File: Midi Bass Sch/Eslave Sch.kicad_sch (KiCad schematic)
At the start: 11 parts, among them SW1 E-slave Reset

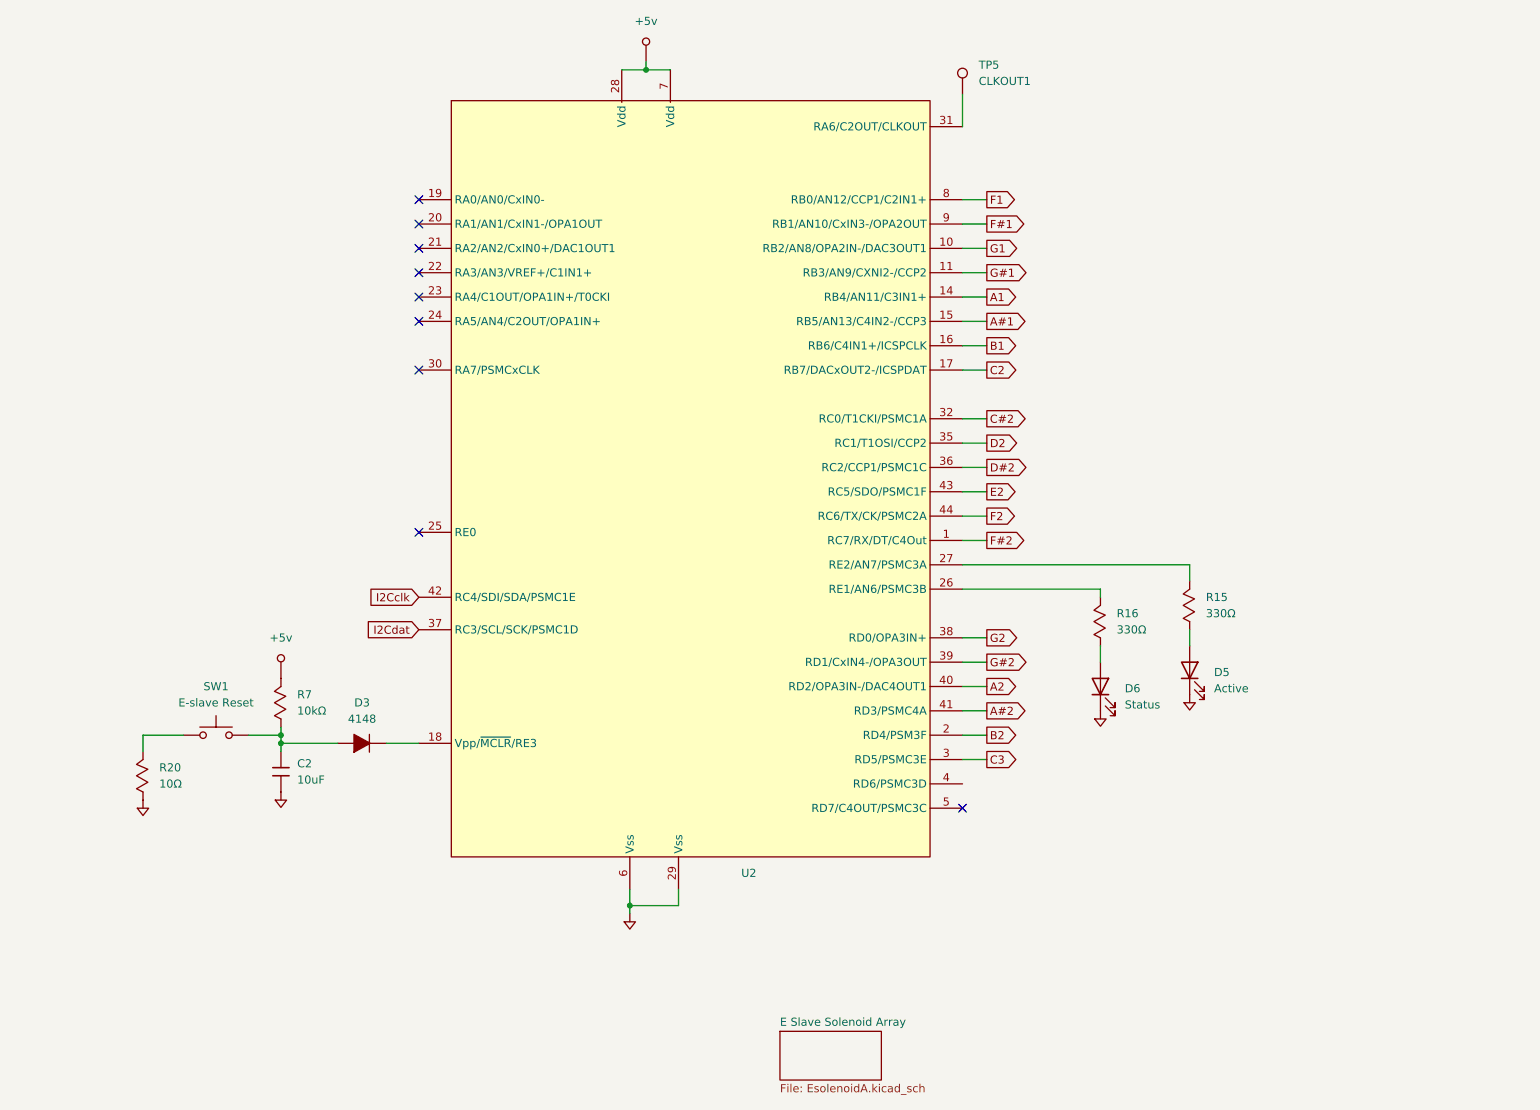
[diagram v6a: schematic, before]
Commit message: added solenoid array for the A slave
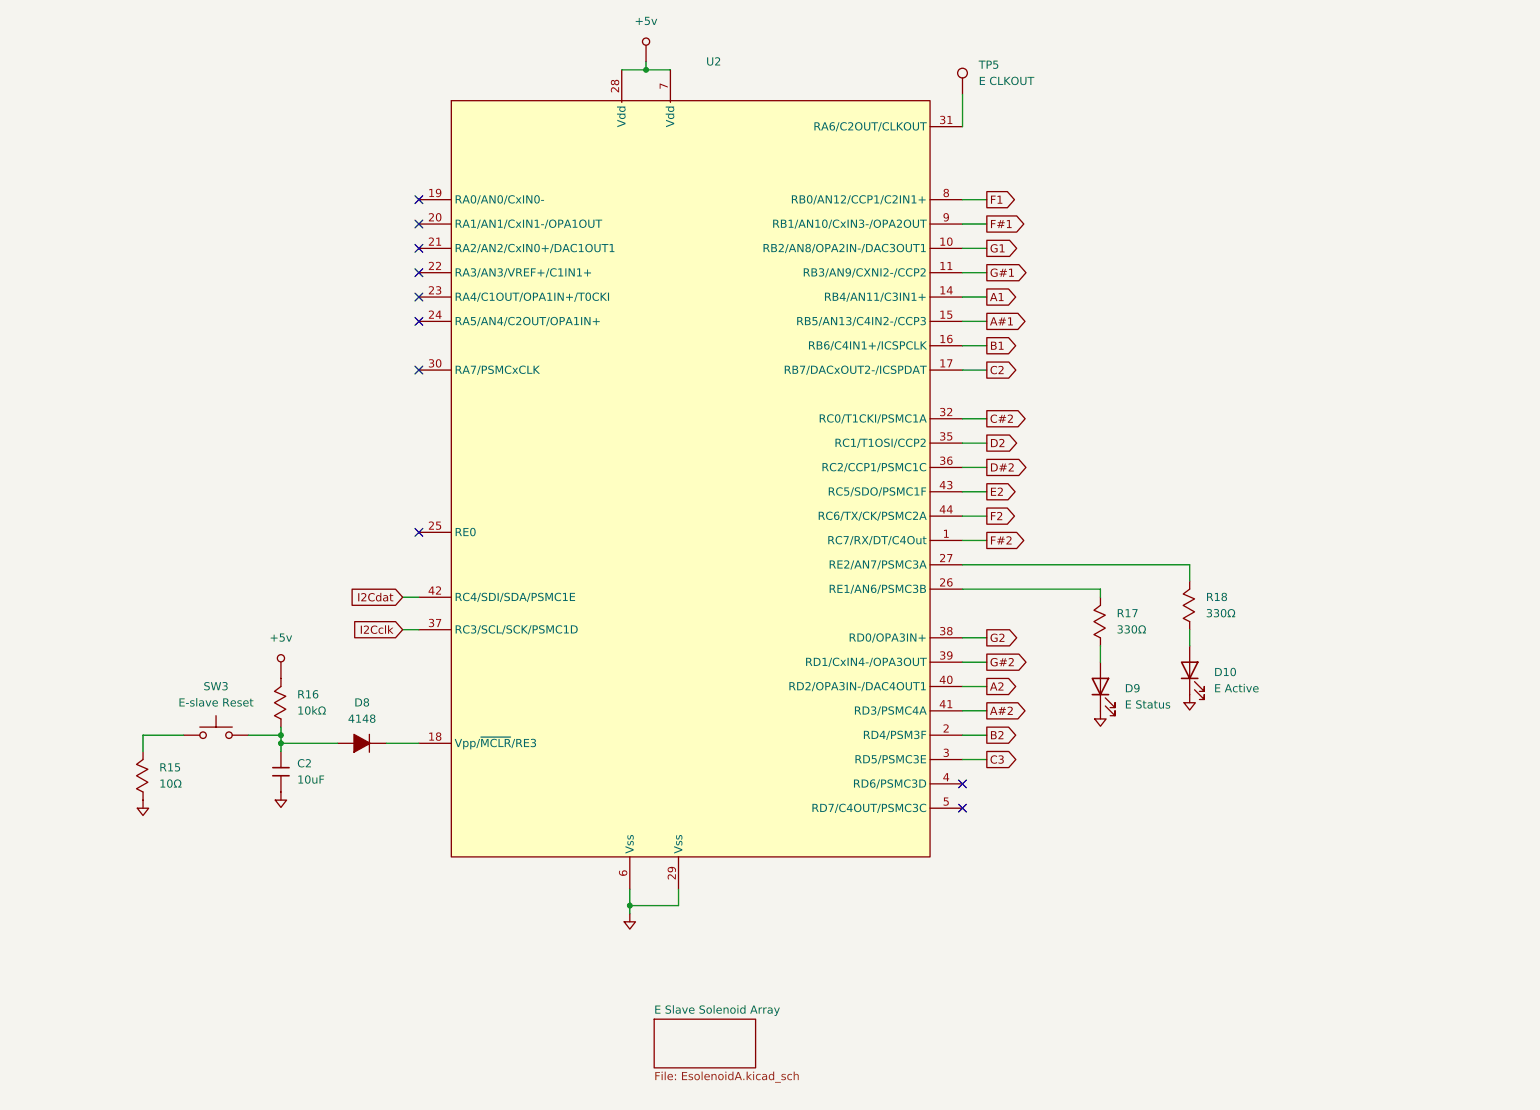
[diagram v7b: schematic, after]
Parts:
- D10: renamed from D5; value Active -> E Active
- D9: renamed from D6; value Status -> E Status
- TP5: value CLKOUT1 -> E CLKOUT
- renumbered D3 to D8, R20 to R15, R7 to R16, R16 to R17, R15 to R18, SW1 to SW3
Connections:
- no-connect marks 9 -> 10
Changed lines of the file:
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@@
 	(generator "eeschema")
 	(generator_version "8.0")
-	(paper "A4")
+	(paper "A")
 	(junction
 		(at 59.69 130.81)
@@
 	)
 	(no_connect
+		(at 166.37 138.43)
+	)
+	(no_connect
 		(at 81.28 73.66)
 	)
@@
 	(wire
 		(pts
+			(xy 78.74 114.3) (xy 81.28 114.3)
+		)
+		(stroke
+			(width 0)
+			(type default)
+		)
+	)
+	(wire
+		(pts
 			(xy 166.37 134.62) (xy 170.18 134.62)
 		)
@@
 		(pts
 			(xy 166.37 130.81) (xy 170.18 130.81)
+		)
+		(stroke
+			(width 0)
+			(type default)
+		)
+	)
+	(wire
+		(pts
+			(xy 78.74 109.22) (xy 81.28 109.22)
 		)
 		(stroke
@@
 	(global_label "I2Cdat"
 		(shape input)
-		(at 81.28 114.3 180)
+		(at 78.74 109.22 180)
 		(fields_autoplaced yes)
 		(effects
@@
 		)
 		(property "Intersheetrefs" "${INTERSHEET_REFS}"
-			(at 72.1868 114.3 0)
+			(at 69.6468 109.22 0)
 			(effects
 				(font
@@
 	(global_label "I2Cclk"
 		(shape input)
-		(at 81.28 109.22 180)
+		(at 78.74 114.3 180)
 		(fields_autoplaced yes)
 		(effects
@@
 		)
 		(property "Intersheetrefs" "${INTERSHEET_REFS}"
-			(at 72.4286 109.22 0)
+			(at 69.8886 114.3 0)
 			(effects
 				(font
@@
 		(dnp no)
 		(fields_autoplaced yes)
-		(property "Reference" "#PWR09"
+		(property "Reference" "#PWR025"
 			(at 114.3 157.48 0)
 			(effects
@@
 			(project "Midi Bass Sch"
 				(path "/06818073-fb22-48ee-acc5-6dedd827034e/55f5fc9c-362b-429f-ad6f-f98ffe4c4860"
-					(reference "#PWR09")
+					(reference "#PWR025")
 					(unit 1)
 				)
@@
 			)
 		)
-		(property "Value" "CLKOUT1"
+		(property "Value" "E CLKOUT"
 			(at 168.91 28.4479 0)
 			(effects
@@
 		(dnp no)
 		(fields_autoplaced yes)
-		(property "Reference" "#PWR018"
+		(property "Reference" "#PWR024"
 			(at 59.69 138.43 0)
 			(effects
@@
 			(project "Midi Bass Sch"
 				(path "/06818073-fb22-48ee-acc5-6dedd827034e/55f5fc9c-362b-429f-ad6f-f98ffe4c4860"
-					(reference "#PWR018")
+					(reference "#PWR024")
 					(unit 1)
 				)
@@
 		(dnp no)
 		(fields_autoplaced yes)
-		(property "Reference" "D5"
+		(property "Reference" "D10"
 			(at 205.74 120.9674 90)
 			(effects
@@
 			)
 		)
-		(property "Value" "Active"
+		(property "Value" "E Active"
 			(at 205.74 123.5074 90)
 			(effects
@@
 			(project ""
 				(path "/06818073-fb22-48ee-acc5-6dedd827034e/55f5fc9c-362b-429f-ad6f-f98ffe4c4860"
-					(reference "D5")
+					(reference "D10")
 					(unit 1)
 				)
@@
 		(dnp no)
 		(fields_autoplaced yes)
-		(property "Reference" "R7"
+		(property "Reference" "R16"
 			(at 62.23 124.4599 90)
 			(effects
@@
 			(project "Midi Bass Sch"
 				(path "/06818073-fb22-48ee-acc5-6dedd827034e/55f5fc9c-362b-429f-ad6f-f98ffe4c4860"
-					(reference "R7")
+					(reference "R16")
 					(unit 1)
 				)
@@
 		(dnp no)
 		(fields_autoplaced yes)
-		(property "Reference" "#PWR045"
+		(property "Reference" "#PWR028"
 			(at 201.93 123.19 0)
 			(effects
@@
 			(project ""
 				(path "/06818073-fb22-48ee-acc5-6dedd827034e/55f5fc9c-362b-429f-ad6f-f98ffe4c4860"
-					(reference "#PWR045")
+					(reference "#PWR028")
 					(unit 1)
 				)
@@
 		(dnp no)
 		(fields_autoplaced yes)
-		(property "Reference" "#PWR051"
+		(property "Reference" "#PWR022"
 			(at 38.1 139.7 0)
 			(effects
@@
 			(project "Midi Bass Sch"
 				(path "/06818073-fb22-48ee-acc5-6dedd827034e/55f5fc9c-362b-429f-ad6f-f98ffe4c4860"
-					(reference "#PWR051")
+					(reference "#PWR022")
 					(unit 1)
 				)
@@
 		(dnp no)
 		(fields_autoplaced yes)
-		(property "Reference" "R20"
+		(property "Reference" "R15"
 			(at 40.64 135.8899 90)
 			(effects
@@
 			(project "Midi Bass Sch"
 				(path "/06818073-fb22-48ee-acc5-6dedd827034e/55f5fc9c-362b-429f-ad6f-f98ffe4c4860"
-					(reference "R20")
+					(reference "R15")
 					(unit 1)
 				)
@@
 		(dnp no)
 		(fields_autoplaced yes)
-		(property "Reference" "SW1"
+		(property "Reference" "SW3"
 			(at 49.53 123.19 0)
 			(effects
@@
 			(project ""
 				(path "/06818073-fb22-48ee-acc5-6dedd827034e/55f5fc9c-362b-429f-ad6f-f98ffe4c4860"
-					(reference "SW1")
+					(reference "SW3")
 					(unit 1)
 				)
@@
 		(dnp no)
 		(fields_autoplaced yes)
-		(property "Reference" "R16"
+		(property "Reference" "R17"
 			(at 190.5 111.7599 90)
 			(effects
@@
 			(project "Midi Bass Sch"
 				(path "/06818073-fb22-48ee-acc5-6dedd827034e/55f5fc9c-362b-429f-ad6f-f98ffe4c4860"
-					(reference "R16")
+					(reference "R17")
 					(unit 1)
 				)
@@
 		(on_board yes)
 		(dnp no)
-		(fields_autoplaced yes)
 		(property "Reference" "U2"
-			(at 131.7341 152.4 0)
+			(at 126.238 25.4 0)
 			(effects
 				(font
@@
 		(dnp no)
 		(fields_autoplaced yes)
-		(property "Reference" "R15"
+		(property "Reference" "R18"
 			(at 204.47 109.2199 90)
 			(effects
@@
 			(project ""
 				(path "/06818073-fb22-48ee-acc5-6dedd827034e/55f5fc9c-362b-429f-ad6f-f98ffe4c4860"
-					(reference "R15")
+					(reference "R18")
 					(unit 1)
 				)
@@
 		(dnp no)
 		(fields_autoplaced yes)
-		(property "Reference" "D3"
+		(property "Reference" "D8"
 			(at 72.39 125.73 90)
 			(effects
@@
 			(project "Midi Bass Sch"
 				(path "/06818073-fb22-48ee-acc5-6dedd827034e/55f5fc9c-362b-429f-ad6f-f98ffe4c4860"
-					(reference "D3")
+					(reference "D8")
 					(unit 1)
 				)
@@
 		(dnp no)
 		(fields_autoplaced yes)
-		(property "Reference" "D6"
+		(property "Reference" "D9"
 			(at 191.77 123.5074 90)
 			(effects
@@
 			)
 		)
-		(property "Value" "Status"
+		(property "Value" "E Status"
 			(at 191.77 126.0474 90)
 			(effects
@@
 			(project "Midi Bass Sch"
 				(path "/06818073-fb22-48ee-acc5-6dedd827034e/55f5fc9c-362b-429f-ad6f-f98ffe4c4860"
-					(reference "D6")
+					(reference "D9")
 					(unit 1)
 				)
@@
 		(dnp no)
 		(fields_autoplaced yes)
-		(property "Reference" "#PWR046"
+		(property "Reference" "#PWR027"
 			(at 187.96 125.73 0)
 			(effects
@@
 			(project "Midi Bass Sch"
 				(path "/06818073-fb22-48ee-acc5-6dedd827034e/55f5fc9c-362b-429f-ad6f-f98ffe4c4860"
-					(reference "#PWR046")
+					(reference "#PWR027")
 					(unit 1)
 				)
@@
 		(dnp no)
 		(fields_autoplaced yes)
-		(property "Reference" "#PWR017"
+		(property "Reference" "#PWR023"
 			(at 64.4144 116.9416 0)
 			(effects
@@
 			(project "Midi Bass Sch"
 				(path "/06818073-fb22-48ee-acc5-6dedd827034e/55f5fc9c-362b-429f-ad6f-f98ffe4c4860"
-					(reference "#PWR017")
+					(reference "#PWR023")
 					(unit 1)
 				)
@@
 		(dnp no)
 		(fields_autoplaced yes)
-		(property "Reference" "#PWR010"
+		(property "Reference" "#PWR026"
 			(at 121.5644 20.4216 0)
 			(effects
@@
 			(project ""
 				(path "/06818073-fb22-48ee-acc5-6dedd827034e/55f5fc9c-362b-429f-ad6f-f98ffe4c4860"
-					(reference "#PWR010")
+					(reference "#PWR026")
 					(unit 1)
 				)
@@
 	)
 	(sheet
-		(at 137.795 177.165)
+		(at 118.11 175.26)
 		(size 15.875 7.62)
 		(fields_autoplaced yes)
@@
 		)
 		(property "Sheetname" "E Slave Solenoid Array"
-			(at 137.795 176.4534 0)
+			(at 118.11 174.5484 0)
 			(effects
 				(font
@@
 		)
 		(property "Sheetfile" "EsolenoidA.kicad_sch"
-			(at 137.795 185.3696 0)
-			(effects
-				(font
+			(at 118.11 183.4646 0)
+			(effects
+				(font

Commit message: added program pins to all processors
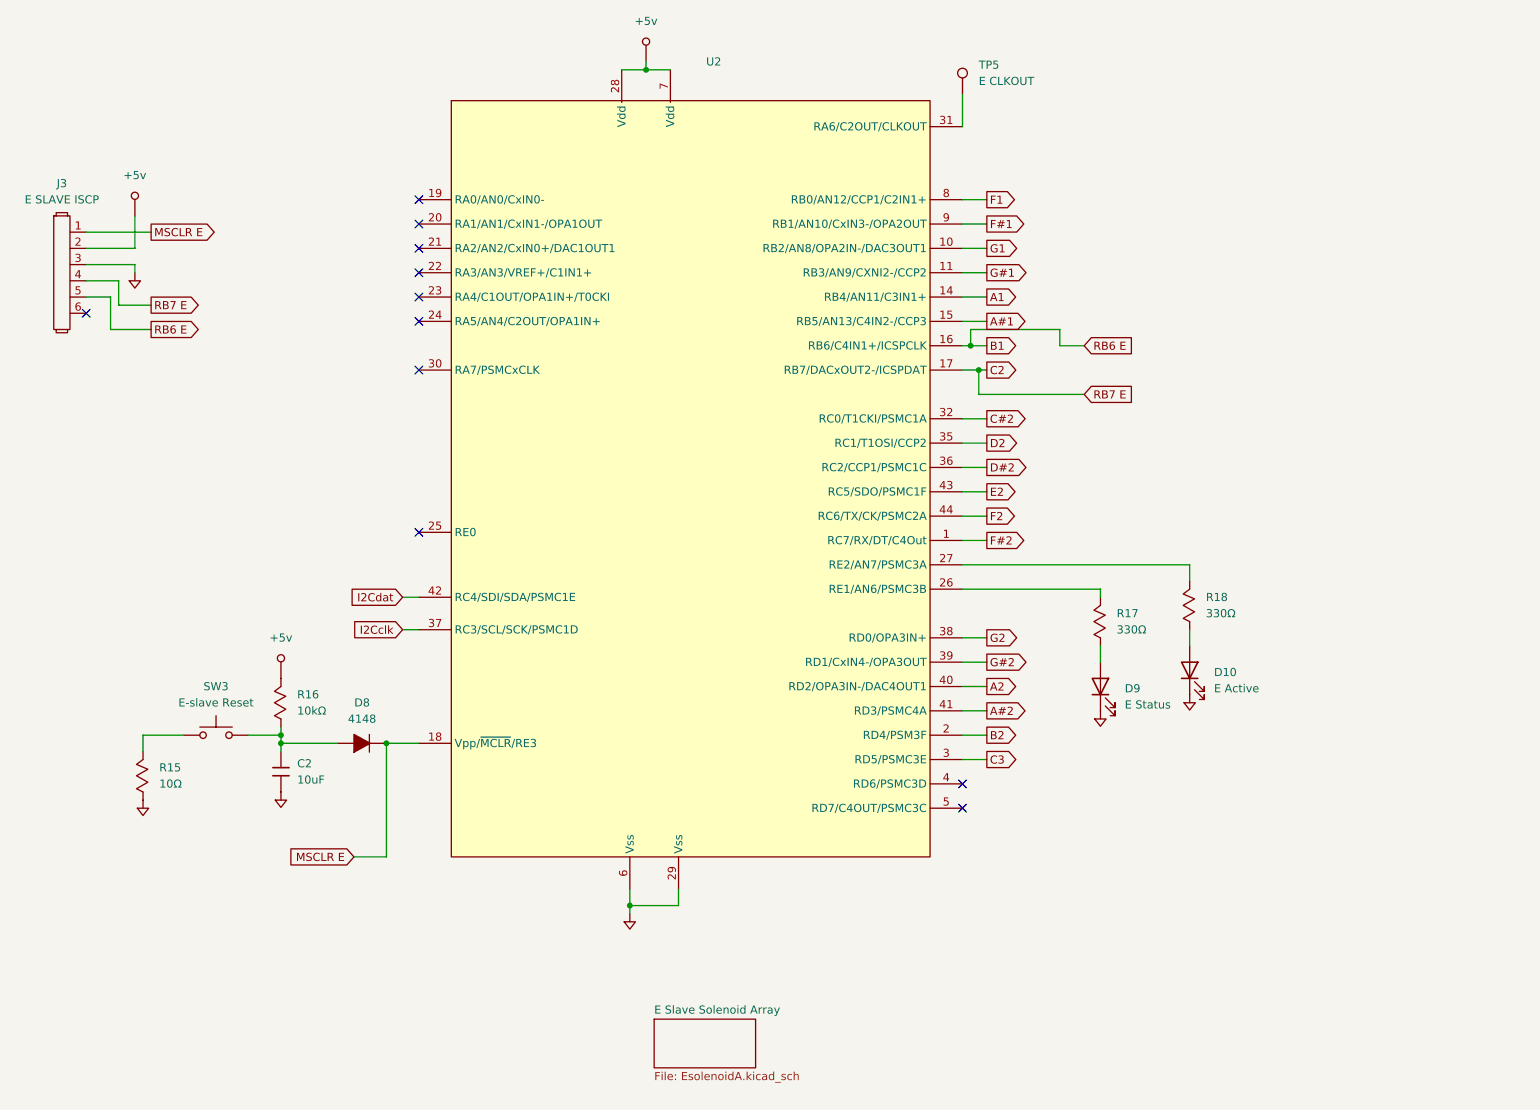
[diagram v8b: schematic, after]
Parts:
- added J3: E SLAVE ISCP, symbol Owen's Symbols:Header_1x6
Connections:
- net +5v: now also J3.2
- net B1: now also J3.5
- net C2: now also J3.4
- net GND: now also J3.3
- net MSCLR E: now reaches D8.2, U2.18 (Vpp/~{MCLR}/RE3)
- net MSCLR E: now also J3.1
- no-connect marks 10 -> 11
